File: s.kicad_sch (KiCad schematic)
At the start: 10 parts, among them J1 USB4085-GF-A_REVB, U1 ESP32-S3-WROOM-1, U2 MCP1825S

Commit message: add supporting stuff and assigned footprints
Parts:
- added D26, D27, D28, D29: ~, LED_SMD:LED_0805_2012Metric_Pad1.15x1.40mm_HandSolder, symbol Device:LED_Small
- added J2: UART connector, Connector_PinHeader_2.54mm:PinHeader_1x04_P2.54mm_Vertical, symbol Connector:Conn_01x04_Pin
- added R2: 10k, Resistor_SMD:R_0805_2012Metric_Pad1.20x1.40mm_HandSolder, symbol Device:R_Small_US
- added R3, R4, R5, R6: 100, Resistor_SMD:R_0805_2012Metric_Pad1.20x1.40mm_HandSolder, symbol Device:R_Small_US
- added SW26: 210-4MS, dip_switch_footprints:DIP8_210-4_CTS, symbol DIP8_210-4_CTS:210-4MS
- C1, C2, C3, C4, C5, C6: footprint (none) -> Capacitor_SMD:C_0805_2012Metric_Pad1.18x1.45mm_HandSolder
- R1: footprint (none) -> Resistor_SMD:R_0805_2012Metric_Pad1.20x1.40mm_HandSolder
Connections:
- net +3.3V: now also J2.1 (Pin_1), R2.1
- net GND: now also J2.4 (Pin_4), R3.2, R4.2, R5.2, R6.2, SW26.1, SW26.2, SW26.3, SW26.4
- net led_2: now reaches U1.10 (IO17)
- net led_2: now also D27.2 (A)
- net led_3: now reaches U1.11 (IO18)
- net led_3: now also D28.2 (A)
- net led_1: now reaches U1.22 (IO14)
- net led_1: now also D26.2 (A)
- net led_4: now reaches U1.23 (IO21)
- net led_4: now also D29.2 (A)
- net at U1.27 (IO0): now also R2.2, SW26.8
- net sw_2: now reaches U1.33 (IO40)
- net sw_2: now also SW26.7
- net sw_3: now reaches U1.34 (IO41)
- net sw_3: now also SW26.6
- net sw_4: now reaches U1.35 (IO42)
- net sw_4: now also SW26.5
- net at U1.36 (RXD0): now also J2.3 (Pin_3)
- net at U1.37 (TXD0): now also J2.2 (Pin_2)
- new net: D26.1 (K), R3.1
- new net: D27.1 (K), R4.1
- new net: D28.1 (K), R5.1
- new net: D29.1 (K), R6.1

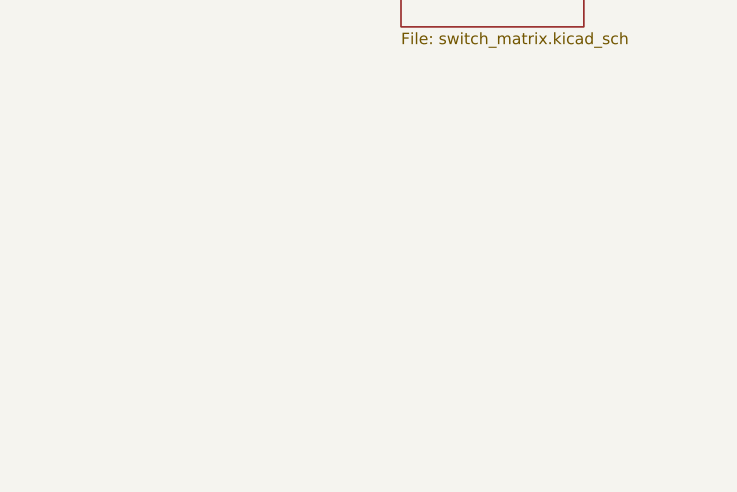
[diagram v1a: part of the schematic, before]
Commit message: copied battery charging schematic
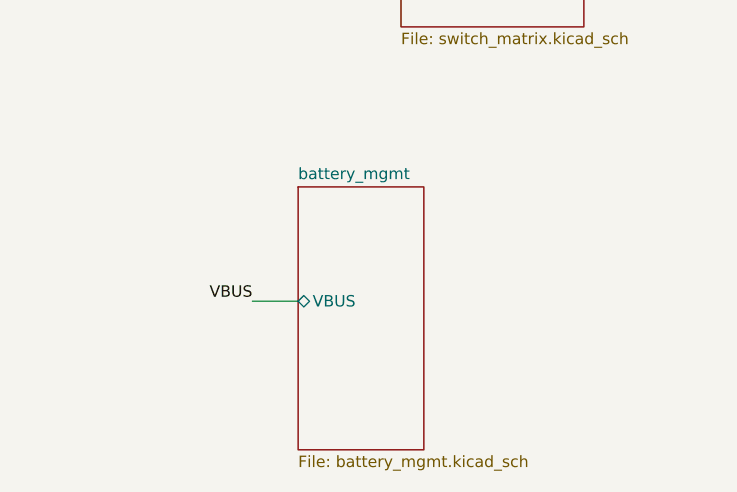
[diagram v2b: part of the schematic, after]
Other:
- added sheet battery_mgmt (battery_mgmt.kicad_sch)
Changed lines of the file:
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@@
 	(wire
 		(pts
+			(xy 240.03 124.46) (xy 245.11 124.46)
+		)
+		(stroke
+			(width 0)
+			(type default)
+		)
+	)
+	(wire
+		(pts
 			(xy 251.46 67.31) (xy 256.54 67.31)
 		)
@@
 		)
 	)
+	(label "VBUS"
+		(at 240.03 124.46 180)
+		(effects
+			(font
+				(size 1.27 1.27)
+			)
+			(justify right bottom)
+		)
+	)
 	(label "USB_D+"
 		(at 179.07 63.5 0)
@@
 				)
 			)
+		)
+	)
+	(sheet
+		(at 245.11 111.76)
+		(size 13.97 29.21)
+		(exclude_from_sim no)
+		(in_bom yes)
+		(on_board yes)
+		(dnp no)
+		(fields_autoplaced yes)
+		(stroke
+			(width 0.1524)
+			(type solid)
+		)
+		(fill
+			(color 0 0 0 0.0000)
+		)
+		(property "Sheetname" "battery_mgmt"
+			(at 245.11 111.0484 0)
+			(effects
+				(font
+					(size 1.27 1.27)
+				)
+				(justify left bottom)
+			)
+		)
+		(property "Sheetfile" "battery_mgmt.kicad_sch"
+			(at 245.11 141.5546 0)
+			(effects
+				(font
+					(size 1.27 1.27)
+				)
+				(justify left top)
+			)
+		)
+		(pin "VBUS" bidirectional
+			(at 245.11 124.46 180)
+			(effects
+				(font
+					(size 1.27 1.27)
+				)
+				(justify left)
+			)
+		)
+		(instances
+			(project "s"
+				(path "/915d30bc-a319-49d8-8691-e2837c0e16bd"
+					(page "3")
+				)
+			)

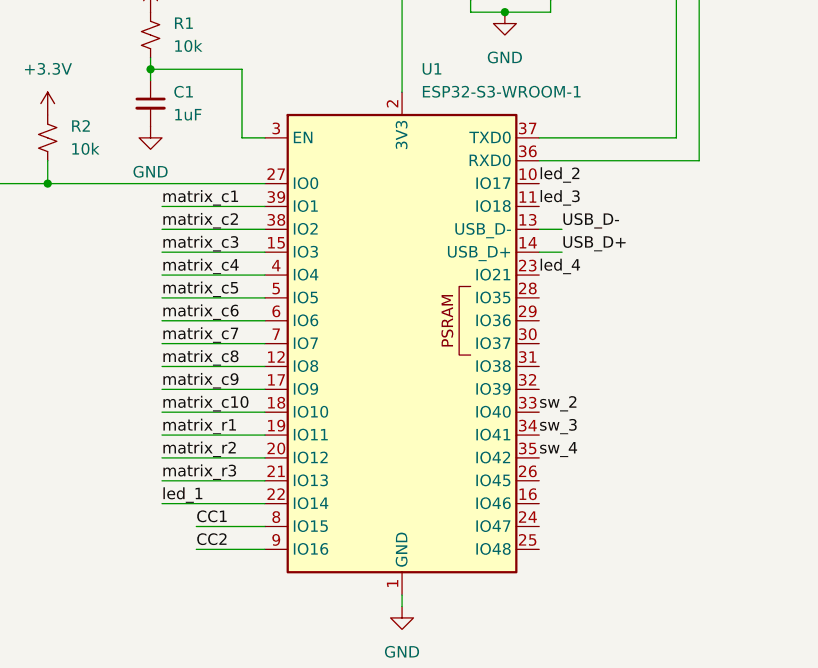
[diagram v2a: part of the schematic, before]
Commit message: routed the key matrix
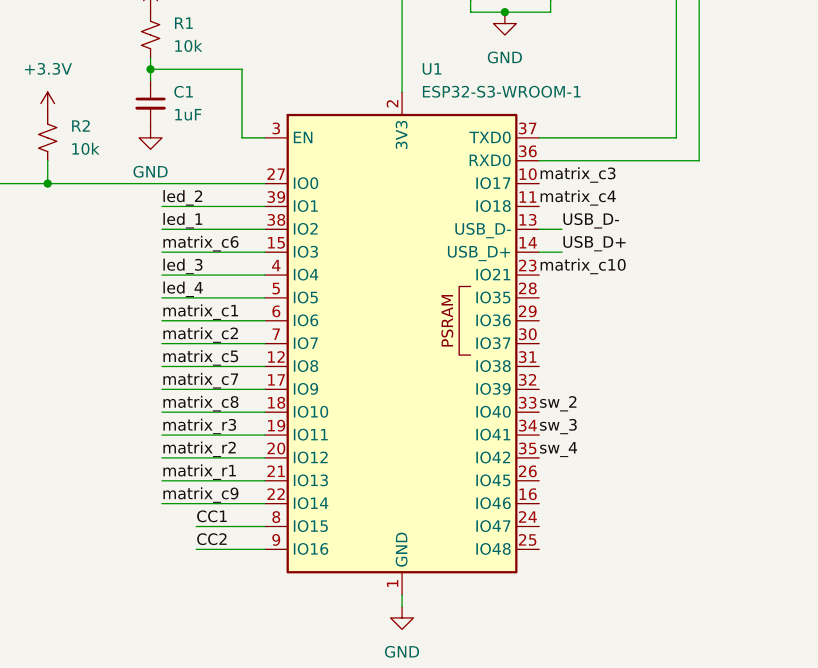
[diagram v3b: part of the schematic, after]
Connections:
- net led_1: now also U1.38 (IO2); no longer U1.22 (IO14)
- net led_2: now also U1.39 (IO1); no longer U1.10 (IO17)
- net led_3: now also U1.4 (IO4); no longer U1.11 (IO18)
- net led_4: now also U1.5 (IO5); no longer U1.23 (IO21)
- net matrix_c1: now also U1.6 (IO6); no longer U1.39 (IO1)
- net matrix_c10: now also U1.23 (IO21); no longer U1.18 (IO10)
- net matrix_c2: now also U1.7 (IO7); no longer U1.38 (IO2)
- net matrix_c3: now also U1.10 (IO17); no longer U1.15 (IO3)
- net matrix_c4: now also U1.11 (IO18); no longer U1.4 (IO4)
- net matrix_c5: now also U1.12 (IO8); no longer U1.5 (IO5)
- net matrix_c6: now also U1.15 (IO3); no longer U1.6 (IO6)
- net matrix_c7: now also U1.17 (IO9); no longer U1.7 (IO7)
- net matrix_c8: now also U1.18 (IO10); no longer U1.12 (IO8)
- net matrix_c9: now also U1.22 (IO14); no longer U1.17 (IO9)
- net matrix_r1: now also U1.21 (IO13); no longer U1.19 (IO11)
- net matrix_r3: now also U1.19 (IO11); no longer U1.21 (IO13)
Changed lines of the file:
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@@
+		)
+	)
+	(label "matrix_c10"
+		(at 176.53 66.04 0)
+		(effects
+			(font
+				(size 1.27 1.27)
+			)
+			(justify left bottom)
 		)
 	)
@@
 	)
 	(label "led_1"
-		(at 134.62 91.44 0)
+		(at 134.62 60.96 0)
 		(effects
 			(font
@@
 		)
 	)
+	(label "matrix_c3"
+		(at 176.53 55.88 0)
+		(effects
+			(font
+				(size 1.27 1.27)
+			)
+			(justify left bottom)
+		)
+	)
 	(label "led_4"
 		(at 90.17 88.9 90)
@@
 		)
 	)
+	(label "matrix_c1"
+		(at 134.62 71.12 0)
+		(effects
+			(font
+				(size 1.27 1.27)
+			)
+			(justify left bottom)
+		)
+	)
 	(label "USB_D+"
 		(at 45.72 45.72 0)
@@
 		)
 	)
-	(label "matrix_c1"
-		(at 134.62 58.42 0)
-		(effects
-			(font
-				(size 1.27 1.27)
-			)
-			(justify left bottom)
-		)
-	)
-	(label "matrix_c2"
-		(at 134.62 60.96 0)
-		(effects
-			(font
-				(size 1.27 1.27)
-			)
-			(justify left bottom)
-		)
-	)
-	(label "matrix_c6"
-		(at 134.62 71.12 0)
-		(effects
-			(font
-				(size 1.27 1.27)
-			)
-			(justify left bottom)
-		)
-	)
-	(label "matrix_c7"
-		(at 134.62 73.66 0)
-		(effects
-			(font
-				(size 1.27 1.27)
-			)
-			(justify left bottom)
-		)
-	)
-	(label "matrix_c3"
-		(at 134.62 63.5 0)
-		(effects
-			(font
-				(size 1.27 1.27)
-			)
-			(justify left bottom)
-		)
-	)
 	(label "matrix_c4"
-		(at 134.62 66.04 0)
-		(effects
-			(font
-				(size 1.27 1.27)
-			)
-			(justify left bottom)
-		)
-	)
-	(label "matrix_c5"
-		(at 134.62 68.58 0)
-		(effects
-			(font
-				(size 1.27 1.27)
-			)
-			(justify left bottom)
-		)
-	)
-	(label "matrix_c8"
-		(at 134.62 76.2 0)
-		(effects
-			(font
-				(size 1.27 1.27)
-			)
-			(justify left bottom)
-		)
-	)
-	(label "matrix_c9"
-		(at 134.62 78.74 0)
-		(effects
-			(font
-				(size 1.27 1.27)
-			)
-			(justify left bottom)
-		)
-	)
-	(label "matrix_c10"
-		(at 134.62 81.28 0)
+		(at 176.53 58.42 0)
 		(effects
 			(font
@@
 		)
 	)
+	(label "matrix_c7"
+		(at 134.62 78.74 0)
+		(effects
+			(font
+				(size 1.27 1.27)
+			)
+			(justify left bottom)
+		)
+	)
+	(label "led_3"
+		(at 134.62 66.04 0)
+		(effects
+			(font
+				(size 1.27 1.27)
+			)
+			(justify left bottom)
+		)
+	)
 	(label "matrix_c1"
 		(at 251.46 24.13 180)
@@
 		)
 	)
+	(label "matrix_c6"
+		(at 134.62 63.5 0)
+		(effects
+			(font
+				(size 1.27 1.27)
+			)
+			(justify left bottom)
+		)
+	)
+	(label "led_2"
+		(at 134.62 58.42 0)
+		(effects
+			(font
+				(size 1.27 1.27)
+			)
+			(justify left bottom)
+		)
+	)
 	(label "CC2"
 		(at 138.43 96.52 0)
@@
 		)
 	)
-	(label "matrix_r1"
+	(label "matrix_r3"
 		(at 134.62 83.82 0)
 		(effects
@@
 		)
 	)
-	(label "matrix_r3"
+	(label "matrix_r1"
 		(at 134.62 88.9 0)
 		(effects
@@
 		)
 	)
+	(label "matrix_c5"
+		(at 134.62 76.2 0)
+		(effects
+			(font
+				(size 1.27 1.27)
+			)
+			(justify left bottom)
+		)
+	)
 	(label "sw_2"
 		(at 96.52 66.04 0)
@@
 		)
 	)
-	(label "led_2"
-		(at 176.53 55.88 0)
-		(effects
-			(font
-				(size 1.27 1.27)
-			)
-			(justify left bottom)
-		)
-	)
-	(label "led_3"
-		(at 176.53 58.42 0)
+	(label "matrix_c9"
+		(at 134.62 91.44 0)
+		(effects
+			(font
+				(size 1.27 1.27)
+			)
+			(justify left bottom)
+		)
+	)
+	(label "matrix_c2"
+		(at 134.62 73.66 0)
 		(effects
 			(font
@@
 	)
 	(label "led_4"
-		(at 176.53 66.04 0)
-		(effects
-			(font
+		(at 134.62 68.58 0)
+		(effects
+			(font
+				(size 1.27 1.27)
+			)
+			(justify left bottom)
+		)
+	)
+	(label "matrix_c8"
+		(at 134.62 81.28 0)
+		(effects
+			(font

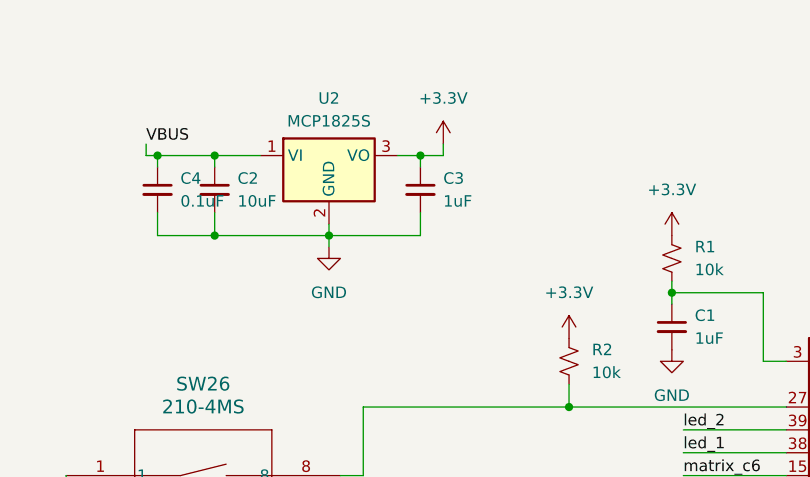
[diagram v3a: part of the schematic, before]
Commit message: quick commit: moved stuff around and deleted a capacitor
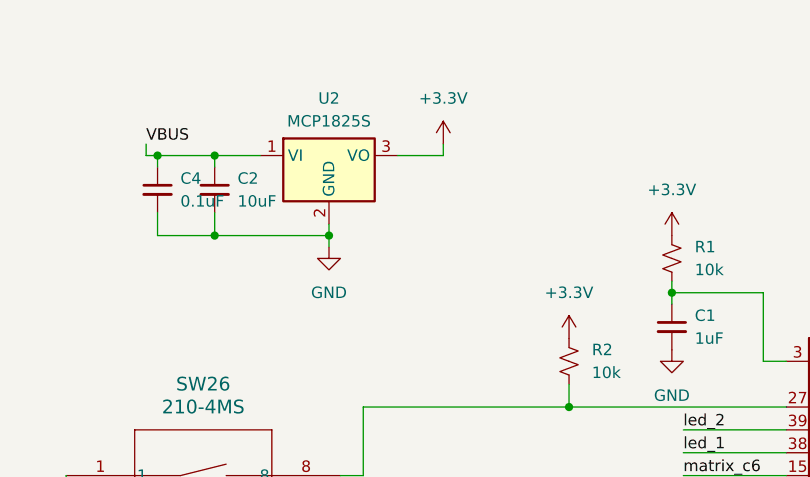
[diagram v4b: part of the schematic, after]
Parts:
- removed C3: 1uF, Capacitor_SMD:C_0805_2012Metric_Pad1.18x1.45mm_HandSolder, symbol Device:C_Small
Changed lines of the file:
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@@
-	)
-	(junction
-		(at 105.41 27.94)
-		(diameter 0)
-		(color 0 0 0 0)
 	)
 	(junction
@@
 	(wire
 		(pts
-			(xy 105.41 34.29) (xy 105.41 36.83)
-		)
-		(stroke
-			(width 0)
-			(type default)
-		)
-	)
-	(wire
-		(pts
 			(xy 217.17 27.94) (xy 217.17 29.21)
 		)
@@
 	(wire
 		(pts
-			(xy 105.41 27.94) (xy 105.41 29.21)
-		)
-		(stroke
-			(width 0)
-			(type default)
-		)
-	)
-	(wire
-		(pts
 			(xy 66.04 66.04) (xy 66.04 68.58)
 		)
@@
 	(wire
 		(pts
-			(xy 105.41 27.94) (xy 107.95 27.94)
-		)
-		(stroke
-			(width 0)
-			(type default)
-		)
-	)
-	(wire
-		(pts
 			(xy 161.29 101.6) (xy 161.29 102.87)
 		)
@@
 	(wire
 		(pts
-			(xy 95.25 36.83) (xy 105.41 36.83)
-		)
-		(stroke
-			(width 0)
-			(type default)
-		)
-	)
-	(wire
-		(pts
 			(xy 134.62 60.96) (xy 146.05 60.96)
 		)
@@
 	(wire
 		(pts
-			(xy 102.87 27.94) (xy 105.41 27.94)
+			(xy 102.87 27.94) (xy 107.95 27.94)
 		)
 		(stroke
@@
 					(unit 1)
 				)
-			)
-		)
-	)
-	(symbol
-		(lib_id "Device:C_Small")
-		(at 105.41 31.75 0)
-		(unit 1)
-		(exclude_from_sim no)
-		(in_bom yes)
-		(on_board yes)
-		(dnp no)
-		(fields_autoplaced yes)
-		(property "Reference" "C3"
-			(at 107.95 30.4862 0)
-			(effects
-				(font
-					(size 1.27 1.27)
-				)
-				(justify left)
-			)
-		)
-		(property "Value" "1uF"
-			(at 107.95 33.0262 0)
-			(effects
-				(font
-					(size 1.27 1.27)
-				)
-				(justify left)
-			)
-		)
-		(property "Footprint" "Capacitor_SMD:C_0805_2012Metric_Pad1.18x1.45mm_HandSolder"
-			(at 105.41 31.75 0)
-			(effects
-				(font
-					(size 1.27 1.27)
-				)
-				(hide yes)
-			)
-		)
-		(property "Datasheet" "~"
-			(at 105.41 31.75 0)
-			(effects
-				(font
-					(size 1.27 1.27)
-				)
-				(hide yes)
-			)
-		)
-		(property "Description" "Unpolarized capacitor, small symbol"
-			(at 105.41 31.75 0)
-			(effects
-				(font
-					(size 1.27 1.27)
-				)
-				(hide yes)
-			)
-		)
-		(pin "1"
-		)
-		(pin "2"
-		)
-		(instances
-			(project ""
-				(path "/915d30bc-a319-49d8-8691-e2837c0e16bd"
-					(reference "C3")
-					(unit 1)
-				)

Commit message: route some more stuff
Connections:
- net UART_TX: now reaches J2.2 (Pin_2), U1.37 (TXD0)
- net UART_RX: now reaches J2.3 (Pin_3), U1.36 (RXD0)
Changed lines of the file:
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@@
+		)
+	)
+	(label "UART_TX"
+		(at 201.93 22.86 0)
+		(effects
+			(font
+				(size 1.27 1.27)
+			)
+			(justify left bottom)
 		)
 	)
@@
 		(effects
 			(font
+				(size 1.27 1.27)
+			)
+			(justify left bottom)
+		)
+	)
+	(label "UART_RX"
+		(at 201.93 25.4 0)
+		(effects
+			(font

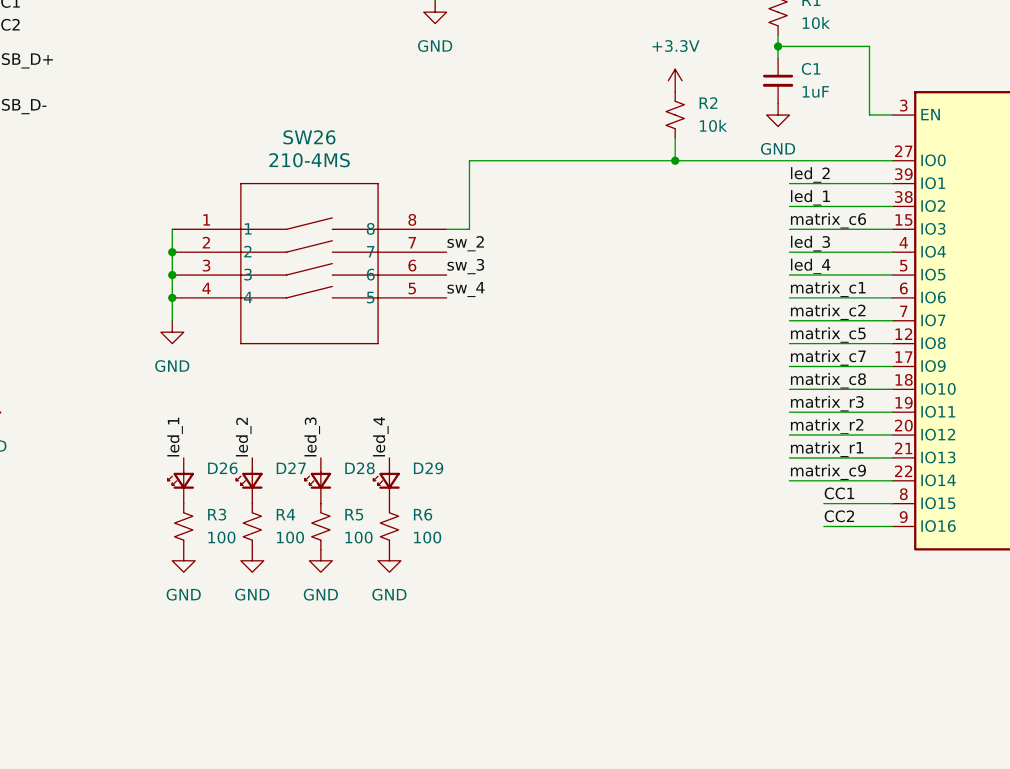
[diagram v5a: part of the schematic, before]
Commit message: remove 2 of the 4 user LEDs
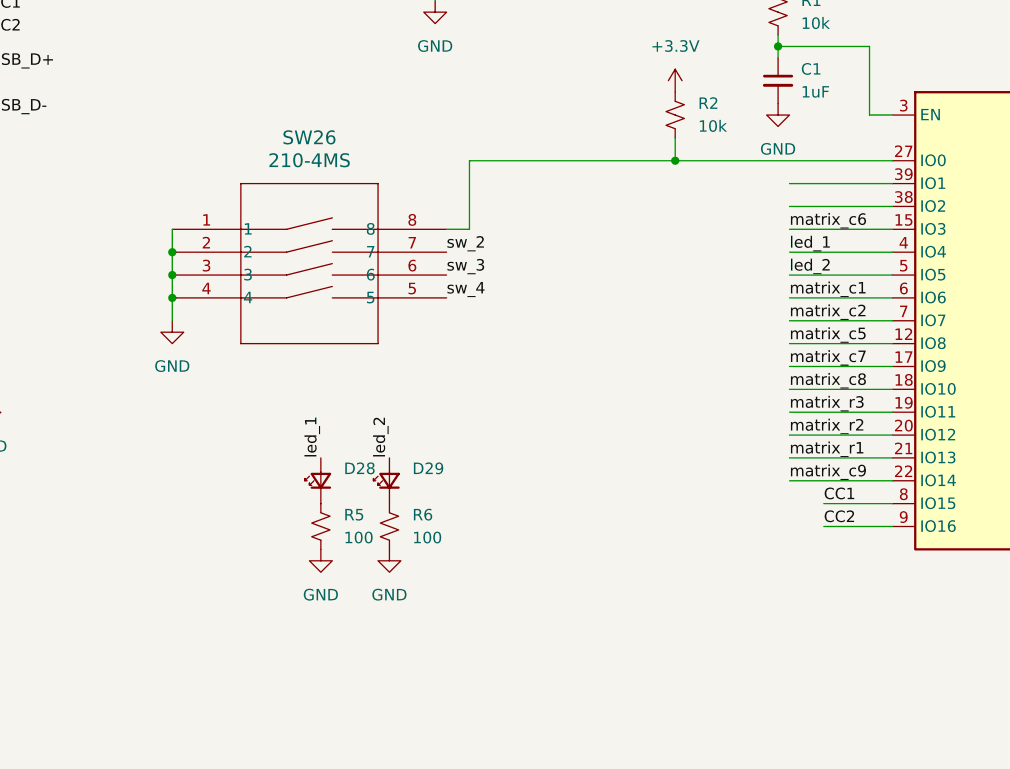
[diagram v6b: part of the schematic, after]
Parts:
- removed D26, D27: ~, LED_SMD:LED_0805_2012Metric_Pad1.15x1.40mm_HandSolder, symbol Device:LED_Small
- removed R3, R4: 100, Resistor_SMD:R_0805_2012Metric_Pad1.20x1.40mm_HandSolder, symbol Device:R_Small_US
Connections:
- net led_3 is gone; now on net led_1: D28.2 (A), U1.4 (IO4)
- net led_4 is gone; now on net led_2: D29.2 (A), U1.5 (IO5)
- net led_1: no longer U1.38 (IO2)
- net led_2: no longer U1.39 (IO1)
